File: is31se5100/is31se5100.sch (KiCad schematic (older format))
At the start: 1 part

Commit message: Added buttons to schematic
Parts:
- added C? (x6): 47nF, symbol Device:C_Small
- added R? (x6): 39k, symbol Device:R_Small
- added U? (x6): MAX7301, symbol Custom_Interface_Expansion:MAX7301
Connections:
- net labels added: BUTTON1, BUTTON10, BUTTON100, BUTTON101, BUTTON102, BUTTON103, BUTTON104, BUTTON105, BUTTON106, BUTTON107, BUTTON108, BUTTON109, BUTTON11, BUTTON110, BUTTON111, BUTTON112, BUTTON113, BUTTON114, BUTTON115, BUTTON116, BUTTON117, BUTTON118, BUTTON119, BUTTON12, BUTTON120, BUTTON121, BUTTON122, BUTTON123, BUTTON124, BUTTON125, BUTTON126, BUTTON127, BUTTON128, BUTTON129, BUTTON13, BUTTON130, BUTTON131, BUTTON132, BUTTON133, BUTTON134, BUTTON135, BUTTON136, BUTTON137, BUTTON138, BUTTON139, BUTTON14, BUTTON140, BUTTON141, BUTTON142, BUTTON143, BUTTON144, BUTTON15, BUTTON16, BUTTON17, BUTTON18, BUTTON19, BUTTON2, BUTTON20, BUTTON21, BUTTON22, BUTTON23, BUTTON24, BUTTON25, BUTTON26, BUTTON27, BUTTON28, BUTTON29, BUTTON3, BUTTON30, BUTTON31, BUTTON32, BUTTON33, BUTTON34, BUTTON35, BUTTON36, BUTTON37, BUTTON38, BUTTON39, BUTTON4, BUTTON40, BUTTON41, BUTTON42, BUTTON43, BUTTON44, BUTTON45, BUTTON46, BUTTON47, BUTTON48, BUTTON49, BUTTON5, BUTTON50, BUTTON51, BUTTON52, BUTTON53, BUTTON54, BUTTON55, BUTTON56, BUTTON57, BUTTON58, BUTTON59, BUTTON6, BUTTON60, BUTTON61, BUTTON62, BUTTON63, BUTTON64, BUTTON65, BUTTON66, BUTTON67, BUTTON68, BUTTON69, BUTTON7, BUTTON70, BUTTON71, BUTTON72, BUTTON73, BUTTON74, BUTTON75, BUTTON76, BUTTON77, BUTTON78, BUTTON79, BUTTON8, BUTTON80, BUTTON81, BUTTON82, BUTTON83, BUTTON84, BUTTON85, BUTTON86, BUTTON87, BUTTON88, BUTTON89, BUTTON9, BUTTON90, BUTTON91, BUTTON92, BUTTON93, BUTTON94, BUTTON95, BUTTON96, BUTTON97, BUTTON98, BUTTON99, SCKL, ~CS
- wire segments 0 -> 48
- no-connect marks 0 -> 24
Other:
- note added: "1 bulk decoupling capacitor\n"
- note added: "1 decoupling capactor 47nF per MAX7301"
- note added: "can leave disconnected output pins on the max7301 because of internal pull-ups\n"

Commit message: Added connections to IS31SE5100 and daisy-linked MAX7301s
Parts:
- removed U?: IS31SE5100, symbol Custom_Sensor_Touch:IS31SE5100
- added C?: 0.1uF, symbol Device:C_Small
- added C?: 10uF, symbol Device:C_Small
- added C? (x8): 5pF, symbol Device:C_Small
- added R? (x8): 510, symbol Device:R_Small
- added R? (x2): 10k, symbol Device:R_Small
- added R? (x2): 4k7, symbol Device:R_Small
- added U?: IS31SE5100-SALS2, symbol Custom_Sensor_Touch:IS31SE5100-SALS2
- added U? (x8): Electrode, symbol Custom_Sensor_Touch:Electrode
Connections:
- net labels added: BUTTON, INTB, MC_INTERRUPT, MC_SCL, MC_SDA, SCL, SDA, SDB
- wire segments 48 -> 142
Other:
- note added: "can leave unused output pins on the max7301 disconnected because of internal pull-ups\n"
- note removed: "can leave disconnected output pins on the max7301 because of internal pull-ups\n"
- moved on the sheet: R?, U?

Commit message: Added control test
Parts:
- added C?: 10uF, symbol Device:C_Small
- added C?: 0.1uF, symbol Device:C_Small
- added C? (x8): 5pF, symbol Device:C_Small
- added C?: 47nF, symbol Device:C_Small
- added D? (x8): G, symbol Device:LED_Small
- added J? (x2): Conn_01x04, symbol Connector_Generic:Conn_01x04
- added JP? (x2): SolderJumper_3_Bridged12, symbol Jumper:SolderJumper_3_Bridged12
- added R? (x8): 510, symbol Device:R_Small
- added R? (x5): 1k, symbol Device:R_Small
- added R? (x3): 4k7, symbol Device:R_Small
- added R?: 39k, symbol Device:R_Small
- added U?: IS31SE5100-SALS2, symbol Custom_Sensor_Touch:IS31SE5100-SALS2
- added U? (x8): Electrode, symbol Custom_Sensor_Touch:Electrode
- added U?: MAX7301, symbol Custom_Interface_Expansion:MAX7301
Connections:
- net +3V3: now also C?.1, C?.1, C?.1, D?.2 (A), D?.2 (A), D?.2 (A), D?.2 (A), D?.2 (A), D?.2 (A), D?.2 (A), D?.2 (A), U?.36 (Vdd), U?.5 (VCC)
- net GND: now also C?.2, C?.2, C?.2, C?.2, C?.2, C?.2, C?.2, C?.2, C?.2, C?.2, C?.2, R?.2, U?.14 (AD), U?.2 (GND), U?.22 (GND), U?.3 (GND), U?.4 (GND)
- new net: R?.2, U?.1 (OUT6)
- new net: R?.1, U?.10 (CAP8)
- new net: R?.1, U?.11 (CAP5)
- new net: R?.1, U?.12 (CAP6)
- new net: R?.1, U?.13 (CAP7)
- new net: R?.2, U?.19 (OUT1)
- new net: JP?.2 (C), U?.2 (OUT7)
- new net: R?.2, U?.20 (OUT2)
- new net: R?.2, U?.21 (OUT3)
- new net: R?.2, U?.23 (OUT4)
- new net: R?.2, U?.24 (OUT5)
- new net: JP?.2 (C), U?.3 (OUT8)
- new net: R?.1, U?.6 (CAP1)
- new net: R?.1, U?.7 (CAP2)
- new net: R?.1, U?.8 (CAP3)
- new net: R?.1, U?.9 (CAP4)
- new net: C?.1, R?.2, U?.~ (x8)
- new net: D?.1 (K), R?.1 (x8)
- new net: JP?.1 (A), R?.2 (x2)
- new net: R?.1, U?.1 (ISET)
- new net: JP?.3 (B), U?.30 (P5)
- new net: JP?.3 (B), U?.32 (P4)
- new net DIN_CTRL: J?.2 (Pin_2), U?.34 (DIN)
- new net DOUT_CTRL: J?.1 (Pin_1), U?.4 (DOUT)
- new net INTB_CTRL: J?.2 (Pin_2), U?.17 (INTB)
- new net SCKL_CTRL: J?.3 (Pin_3), U?.33 (SCKL)
- new net SCL_CTRL: J?.4 (Pin_4), U?.15 (SCL)
- new net SDA_CTRL: J?.3 (Pin_3), U?.16 (SDA)
- new net SDB_CTRL: J?.1 (Pin_1), U?.18 (SDB)
- new net ~CS_CTRL: J?.4 (Pin_4), U?.35 (~CS)
- no-connect marks 24 -> 50
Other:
- note added: "Control that tests one IS31SE5100 and one MAX7301 with jumpers\n"
- note added: "INTB is an interrupt line that is open drain"
- moved on the sheet: C?, R?, U?

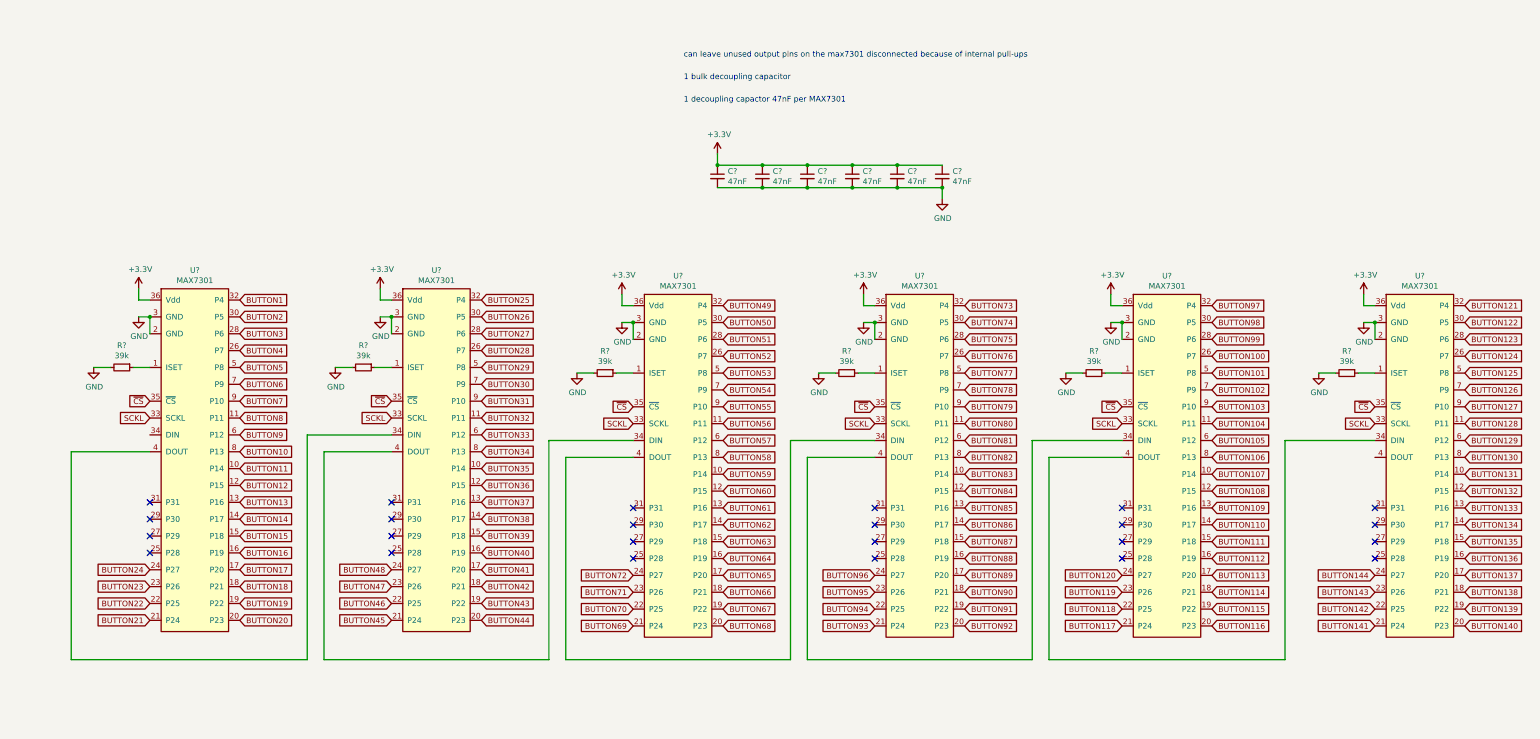
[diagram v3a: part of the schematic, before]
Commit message: Simplified by reducing number of IS31SE5100
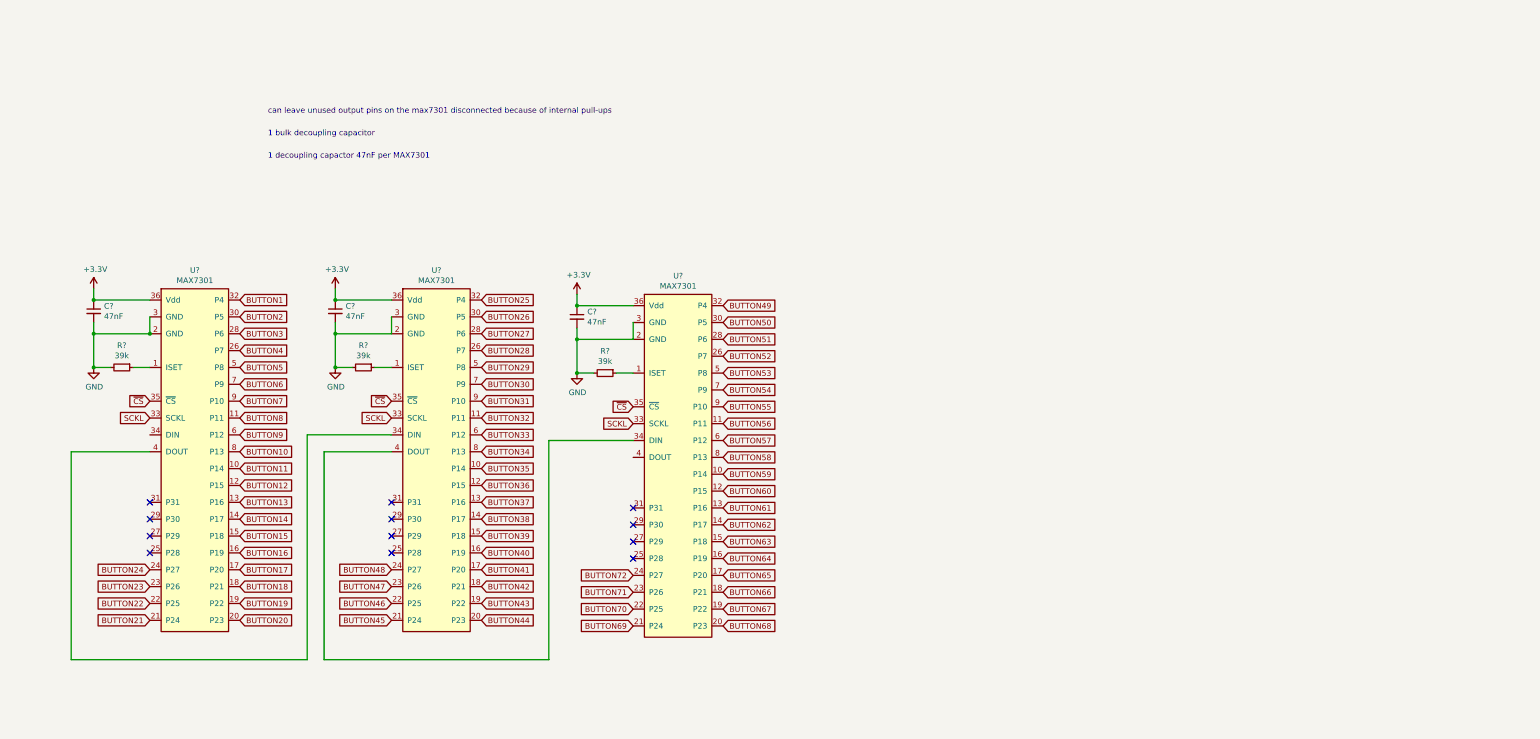
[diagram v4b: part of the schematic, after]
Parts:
- removed C? (x6): 47nF, symbol Device:C_Small
- removed R? (x6): 39k, symbol Device:R_Small
- removed U? (x3): MAX7301, symbol Custom_Interface_Expansion:MAX7301
- added C? (x3): 47nF, symbol Device:C_Small
- added R? (x3): 39k, symbol Device:R_Small
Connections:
- net +3V3: now also C?.1, C?.1, C?.1
- net GND: now also C?.2, C?.2, C?.2, R?.2, R?.2, R?.2
- net at U?.1 (ISET): now also R?.1 (x3)
- no-connect marks 50 -> 38

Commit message: Added pull-ups for I2C and INTB
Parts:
- removed R?: 10k, symbol Device:R_Small
- removed R? (x2): 4k7, symbol Device:R_Small
- added C? (x8): 10uF, symbol Device:C_Small
- added C? (x8): 0.1uF, symbol Device:C_Small
- added C? (x64): 5pF, symbol Device:C_Small
- added R? (x64): 510, symbol Device:R_Small
- added R? (x24): 4k7, symbol Device:R_Small
- added R? (x10): 10k, symbol Device:R_Small
- added R? (x2): 2k2, symbol Device:R_Small
- added U? (x8): IS31SE5100-SALS2, symbol Custom_Sensor_Touch:IS31SE5100-SALS2
- added U? (x64): Electrode, symbol Custom_Sensor_Touch:Electrode
- added U? (x3): PCA9546APW, symbol Custom_Interface_Expansion:PCA9546APW
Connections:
- net +3V3: now also C?.1, C?.1, C?.1, C?.1, C?.1, C?.1, C?.1, C?.1, C?.1, C?.1, C?.1, C?.1, C?.1, C?.1, C?.1, C?.1, R?.1, R?.1, R?.1, R?.1, R?.1, R?.1, R?.1, R?.1, R?.1, R?.1, R?.1, R?.1, R?.1, R?.1, R?.1, R?.1, R?.1, R?.1, R?.1, R?.1, R?.1, R?.1, R?.1, R?.1, R?.1, R?.1, R?.2, R?.2, R?.2, R?.2, R?.2, R?.2, R?.2, R?.2, R?.2, R?.2, U?.1 (A0), U?.16 (VDD), U?.16 (VDD), U?.16 (VDD), U?.2 (A1), U?.5 (VCC), U?.5 (VCC), U?.5 (VCC), U?.5 (VCC), U?.5 (VCC), U?.5 (VCC), U?.5 (VCC), U?.5 (VCC)
- net BUTTON1: now also U?.19 (OUT1)
- net BUTTON10: now also U?.20 (OUT2)
- net BUTTON11: now also U?.21 (OUT3)
- net BUTTON12: now also U?.23 (OUT4)
- net BUTTON13: now also U?.24 (OUT5)
- net BUTTON14: now also U?.1 (OUT6)
- net BUTTON15: now also U?.2 (OUT7)
- net BUTTON16: now also U?.3 (OUT8)
- net BUTTON17: now also U?.19 (OUT1)
- net BUTTON18: now also U?.20 (OUT2)
- net BUTTON19: now also U?.21 (OUT3)
- net BUTTON2: now also U?.20 (OUT2)
- net BUTTON20: now also U?.23 (OUT4)
- net BUTTON21: now also U?.24 (OUT5)
- net BUTTON22: now also U?.1 (OUT6)
- net BUTTON23: now also U?.2 (OUT7)
- net BUTTON24: now also U?.3 (OUT8)
- net BUTTON25: now also U?.19 (OUT1)
- net BUTTON26: now also U?.20 (OUT2)
- net BUTTON27: now also U?.21 (OUT3)
- net BUTTON28: now also U?.23 (OUT4)
- net BUTTON29: now also U?.24 (OUT5)
- net BUTTON3: now also U?.21 (OUT3)
- net BUTTON30: now also U?.1 (OUT6)
- net BUTTON31: now also U?.2 (OUT7)
- net BUTTON32: now also U?.3 (OUT8)
- net BUTTON33: now also U?.19 (OUT1)
- net BUTTON34: now also U?.20 (OUT2)
- net BUTTON35: now also U?.21 (OUT3)
- net BUTTON36: now also U?.23 (OUT4)
- net BUTTON37: now also U?.24 (OUT5)
- net BUTTON38: now also U?.1 (OUT6)
- net BUTTON39: now also U?.2 (OUT7)
- net BUTTON4: now also U?.23 (OUT4)
- net BUTTON40: now also U?.3 (OUT8)
- net BUTTON41: now also U?.19 (OUT1)
- net BUTTON42: now also U?.20 (OUT2)
- net BUTTON43: now also U?.21 (OUT3)
- net BUTTON44: now also U?.23 (OUT4)
- net BUTTON45: now also U?.24 (OUT5)
- net BUTTON46: now also U?.1 (OUT6)
- net BUTTON47: now also U?.2 (OUT7)
- net BUTTON48: now also U?.3 (OUT8)
- net BUTTON49: now also U?.19 (OUT1)
- net BUTTON5: now also U?.24 (OUT5)
- net BUTTON50: now also U?.20 (OUT2)
- net BUTTON51: now also U?.21 (OUT3)
- net BUTTON52: now also U?.23 (OUT4)
- net BUTTON53: now also U?.24 (OUT5)
- net BUTTON54: now also U?.1 (OUT6)
- net BUTTON55: now also U?.2 (OUT7)
- net BUTTON56: now also U?.3 (OUT8)
- net BUTTON57: now also U?.19 (OUT1)
- net BUTTON58: now also U?.20 (OUT2)
- net BUTTON59: now also U?.21 (OUT3)
- net BUTTON6: now also U?.1 (OUT6)
- net BUTTON60: now also U?.23 (OUT4)
- net BUTTON61: now also U?.24 (OUT5)
- net BUTTON62: now also U?.1 (OUT6)
- net BUTTON63: now also U?.2 (OUT7)
- net BUTTON64: now also U?.3 (OUT8)
- net BUTTON65: now also U?.19 (OUT1)
- net BUTTON66: now also U?.20 (OUT2)
- net BUTTON67: now also U?.21 (OUT3)
- net BUTTON68: now also U?.23 (OUT4)
- net BUTTON69: now also U?.24 (OUT5)
- net BUTTON7: now also U?.2 (OUT7)
- net BUTTON70: now also U?.1 (OUT6)
- net BUTTON71: now also U?.2 (OUT7)
- net BUTTON72: now also U?.3 (OUT8)
- net BUTTON8: now also U?.3 (OUT8)
- net BUTTON9: now also U?.19 (OUT1)
- net GND: now also C?.2, C?.2, C?.2, C?.2, C?.2, C?.2, C?.2, C?.2, C?.2, C?.2, C?.2, C?.2, C?.2, C?.2, C?.2, C?.2, C?.2, C?.2, C?.2, C?.2, C?.2, C?.2, C?.2, C?.2, C?.2, C?.2, C?.2, C?.2, C?.2, C?.2, C?.2, C?.2, C?.2, C?.2, C?.2, C?.2, C?.2, C?.2, C?.2, C?.2, C?.2, C?.2, C?.2, C?.2, C?.2, C?.2, C?.2, C?.2, C?.2, C?.2, C?.2, C?.2, C?.2, C?.2, C?.2, C?.2, C?.2, C?.2, C?.2, C?.2, C?.2, C?.2, C?.2, C?.2, C?.2, C?.2, C?.2, C?.2, C?.2, C?.2, C?.2, C?.2, C?.2, C?.2, C?.2, C?.2, C?.2, C?.2, C?.2, C?.2, U?.1 (A0), U?.1 (A0), U?.13 (A2), U?.13 (A2), U?.13 (A2), U?.14 (AD), U?.14 (AD), U?.14 (AD), U?.14 (AD), U?.14 (AD), U?.14 (AD), U?.14 (AD), U?.14 (AD), U?.2 (A1), U?.2 (A1), U?.22 (GND), U?.22 (GND), U?.22 (GND), U?.22 (GND), U?.22 (GND), U?.22 (GND), U?.22 (GND), U?.22 (GND), U?.4 (GND), U?.4 (GND), U?.4 (GND), U?.4 (GND), U?.4 (GND), U?.4 (GND), U?.4 (GND), U?.4 (GND), U?.8 (VSS), U?.8 (VSS), U?.8 (VSS)
- net SDB_CTRL: no longer U?.18 (SDB)
- removed net BUTTON: U?.1 (OUT6), U?.19 (OUT1), U?.2 (OUT7), U?.20 (OUT2), U?.21 (OUT3), U?.23 (OUT4), U?.24 (OUT5), U?.3 (OUT8)
- net INTB renamed INTB1
- net INTB1: now also U?.17 (INTB), U?.17 (INTB), U?.17 (INTB), U?.17 (INTB), U?.17 (INTB), U?.17 (INTB), U?.17 (INTB), U?.17 (INTB)
- net MC_SCL renamed M_SCL1
- net M_SCL1: now also R?.2, U?.5 (SC0)
- net MC_SDA renamed M_SDA1
- net M_SDA1: now also R?.2, U?.4 (SD0)
- net SDB: no longer names the net of U?.18 (SDB)
- net SDB: now also R?.1
- new net: R?.1, U?.18 (SDB) (x9)
- new net: R?.1, U?.10 (CAP8) (x8)
- new net: R?.1, U?.11 (CAP5) (x8)
- new net: R?.1, U?.12 (CAP6) (x8)
- new net: R?.1, U?.13 (CAP7) (x8)
- new net: R?.1, U?.6 (CAP1) (x8)
- new net: R?.1, U?.7 (CAP2) (x8)
- new net: R?.1, U?.8 (CAP3) (x8)
- new net: R?.1, U?.9 (CAP4) (x8)
- new net: C?.1, R?.2, U?.~ (x64)
- new net: R?.2, U?.11 (SD3) (x3)
- new net: R?.2, U?.12 (SC3) (x3)
- new net M_SCL2: R?.2, U?.15 (SCL), U?.6 (SD1)
- new net M_SCL3: R?.2, U?.10 (SC2), U?.15 (SCL)
- new net M_SCL4: R?.2, U?.15 (SCL), U?.5 (SC0)
- new net M_SCL5: R?.2, U?.15 (SCL), U?.6 (SD1)
- new net M_SCL6: R?.2, U?.10 (SC2), U?.15 (SCL)
- new net M_SCL7: R?.2, U?.15 (SCL), U?.5 (SC0)
- new net M_SCL8: R?.2, U?.15 (SCL), U?.6 (SD1)
- new net M_SCL9: R?.2, U?.10 (SC2), U?.15 (SCL)
- new net M_SDA2: R?.2, U?.16 (SDA), U?.7 (SC1)
- new net M_SDA3: R?.2, U?.16 (SDA), U?.9 (SD2)
- new net M_SDA4: R?.2, U?.16 (SDA), U?.4 (SD0)
- new net M_SDA5: R?.2, U?.16 (SDA), U?.7 (SC1)
- new net M_SDA6: R?.2, U?.16 (SDA), U?.9 (SD2)
- new net M_SDA7: R?.2, U?.16 (SDA), U?.4 (SD0)
- new net M_SDA8: R?.2, U?.16 (SDA), U?.7 (SC1)
- new net M_SDA9: R?.2, U?.16 (SDA), U?.9 (SD2)
- new net SCL1: R?.2, U?.14 (SCL), U?.14 (SCL), U?.14 (SCL)
- new net SDA1: R?.2, U?.15 (SDA), U?.15 (SDA), U?.15 (SDA)
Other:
- note added: "1 bulk decoupling capacitor (each?)\n"
- note added: "STM32L476RG is 3.3V and we want possible I2C Fast Mode"
- note removed: "1 bulk decoupling capacitor\n"
- moved on the sheet: C?, D?, J?, JP?, R?, U?

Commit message: Preparation for power
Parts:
- removed J?: Conn_01x04, symbol Connector_Generic:Conn_01x04
- added D?: G, symbol Device:LED_Small
- added J?: Conn_01x03, symbol Connector_Generic:Conn_01x03
- added R?: 1k, symbol Device:R_Small
- added R? (x2): 2k2, symbol Device:R_Small
- D? (x8): value G -> Y
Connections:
- net +3V3: now also D?.2 (A), R?.1, R?.1
- net GND: now also R?.2
- net INTB_CTRL: now also J?.1 (Pin_1)
- net SCL_CTRL: now also J?.3 (Pin_3), R?.2
- net SDA_CTRL: now also J?.2 (Pin_2), R?.2
- new net: D?.1 (K), R?.1
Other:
- note added: "1 bulk decoupling capacitor?\n"
- note added: "Power supply"
- note removed: "1 bulk decoupling capacitor (each?)\n"
- moved on the sheet: C?, D?, J?, JP?, R?, U?

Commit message: Added power circuit and extraneous parts
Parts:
- removed C? (x72): 5pF, symbol Device:C_Small
- removed D?: G, symbol Device:LED_Small
- removed R? (x27): 4k7, symbol Device:R_Small
- removed R?: 1k, symbol Device:R_Small
- removed U? (x8): Electrode, symbol Custom_Sensor_Touch:Electrode
- added C? (x10): 10nF, symbol Device:C_Small
- added C? (x14): 10uF, symbol Device:C_Small
- added C? (x8): 5pF, symbol Device:C_Small
- added C? (x8): 10pF, symbol Device:C_Small
- added C? (x8): 15pF, symbol Device:C_Small
- added C? (x8): 1nF, symbol Device:C_Small
- added C? (x8): 5nF, symbol Device:C_Small
- added C? (x8): 1pF, symbol Device:C_Small
- added C? (x8): 15nF, symbol Device:C_Small
- added C? (x8): 25nF, symbol Device:C_Small
- added C? (x8): 50nF, symbol Device:C_Small
- added C? (x8): 1uF, symbol Device:C_Small
- added C? (x8): 5uF, symbol Device:C_Small
- added C? (x8): 15uF, symbol Device:C_Small
- added C? (x8): 25uF, symbol Device:C_Small
- added C? (x8): 50uF, symbol Device:C_Small
- added C? (x72): 6pF, symbol Device:C_Small
- added C? (x8): 100nF, symbol Device:C_Small
- added C? (x8): 20pF, symbol Device:C_Small
- added C? (x8): 22pF, symbol Device:C_Small
- added C? (x8): 18pF, symbol Device:C_Small
- added D?: G, symbol Device:LED_Small
- added D? (x4): B5819W, symbol Device:D_Schottky_Small
- added D?: B, symbol Device:LED_Small
- added F? (x2): 250mA, symbol Device:Polyfuse_Small
- added FB? (x2): 600 @ 600MHz, symbol Device:Ferrite_Bead_Small
- added J? (x16): Conn_01x08, symbol Connector_Generic:Conn_01x08
- added J?: Conn_01x04, symbol Connector_Generic:Conn_01x04
- added JP? (x14): SolderJumper_3_Bridged12, symbol Jumper:SolderJumper_3_Bridged12
- added L? (x2): 10uH, symbol Device:L_Small
- added Q? (x2): AO3401A, Package_TO_SOT_SMD:SOT-23, symbol Transistor_FET:AO3401A
- added R? (x13): 1k, symbol Device:R_Small
- added R? (x36): 2k2, symbol Device:R_Small
- added R? (x10): 100k, symbol Device:R_Small
- added R? (x2): 68k, symbol Device:R_Small
- added R? (x10): 47k, symbol Device:R_Small
- added R? (x10): 15k, symbol Device:R_Small
- added R? (x10): 270, symbol Device:R_Small
- added R? (x8): 1, symbol Device:R_Small
- added R? (x8): 10, symbol Device:R_Small
- added R? (x8): 100, symbol Device:R_Small
- added R? (x8): 10k, symbol Device:R_Small
- added R? (x8): 1.5, symbol Device:R_Small
- added R? (x8): 15, symbol Device:R_Small
- added R? (x8): 150, symbol Device:R_Small
- added R? (x8): 1k5, symbol Device:R_Small
- added R? (x8): 150k, symbol Device:R_Small
- added R? (x8): 2.2, symbol Device:R_Small
- added R? (x8): 22, symbol Device:R_Small
- added R? (x8): 220, symbol Device:R_Small
- added R? (x8): 22k, symbol Device:R_Small
- added R? (x8): 220k, symbol Device:R_Small
- added R? (x8): 2.7, symbol Device:R_Small
- added R? (x8): 27, symbol Device:R_Small
- added R? (x8): 2k7, symbol Device:R_Small
- added R? (x8): 27k, symbol Device:R_Small
- added R? (x8): 270k, symbol Device:R_Small
- added R? (x8): 3.3, symbol Device:R_Small
- added R? (x8): 33, symbol Device:R_Small
- added R? (x8): 330, symbol Device:R_Small
- added R? (x8): 3k3, symbol Device:R_Small
- added R? (x8): 33k, symbol Device:R_Small
- added R? (x8): 330k, symbol Device:R_Small
- added R? (x8): 3.9, symbol Device:R_Small
- added R? (x8): 39, symbol Device:R_Small
- added R? (x8): 390, symbol Device:R_Small
- added R? (x8): 3k9, symbol Device:R_Small
- added R? (x8): 39k, symbol Device:R_Small
- added R? (x8): 390k, symbol Device:R_Small
- added R? (x8): 4.7, symbol Device:R_Small
- added R? (x8): 47, symbol Device:R_Small
- added R? (x8): 470, symbol Device:R_Small
- added R? (x8): 4k7, symbol Device:R_Small
- added R? (x8): 470k, symbol Device:R_Small
- added R? (x8): 5.1, symbol Device:R_Small
- added R? (x8): 51, symbol Device:R_Small
- added R? (x8): 510, symbol Device:R_Small
- added R? (x8): 5k1, symbol Device:R_Small
- added R? (x8): 51k, symbol Device:R_Small
- added R? (x8): 510k, symbol Device:R_Small
- added R? (x8): 120, symbol Device:R_Small
- added R? (x8): 180, symbol Device:R_Small
- added R? (x8): 250, symbol Device:R_Small
- added R? (x8): 300, symbol Device:R_Small
- added R? (x8): 360, symbol Device:R_Small
- added R? (x8): 430, symbol Device:R_Small
- added R? (x8): 1M, symbol Device:R_Small
- added R? (x8): 0, symbol Device:R_Small
- added U? (x128): Electrode, symbol Custom_Sensor_Touch:Electrode
- added U? (x2): MP2359DT-LF, symbol Custom_Power:MP2359DT-LF
- C? (x8): value 5pF -> 6pF
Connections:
- net +3V3: now also C?.1, C?.1, D?.2 (A), L?.2, R?.1, R?.1, R?.1, R?.1, R?.1, R?.1, R?.1, R?.1, R?.1, R?.1, R?.1, R?.1, R?.1, R?.1, R?.1, R?.1, R?.1, R?.1, R?.1, R?.1, R?.1, R?.1, R?.1, R?.1, R?.1, R?.1, R?.1, R?.1, R?.1; no longer C?.1, C?.1, C?.1, D?.2 (A), D?.2 (A), D?.2 (A), D?.2 (A), D?.2 (A), D?.2 (A), D?.2 (A), D?.2 (A), R?.1, R?.1, U?.36 (Vdd), U?.5 (VCC)
- net GND: now also C?.2, C?.2, C?.2, C?.2, C?.2, C?.2, C?.2, C?.2, C?.2, C?.2, C?.2, C?.2, C?.2, C?.2, C?.2, C?.2, C?.2, C?.2, C?.2, C?.2, C?.2, C?.2, C?.2, C?.2, C?.2, C?.2, C?.2, C?.2, C?.2, C?.2, C?.2, C?.2, C?.2, C?.2, C?.2, C?.2, C?.2, C?.2, C?.2, C?.2, C?.2, C?.2, C?.2, C?.2, C?.2, C?.2, C?.2, C?.2, C?.2, C?.2, C?.2, C?.2, C?.2, C?.2, C?.2, C?.2, C?.2, C?.2, C?.2, C?.2, C?.2, C?.2, C?.2, C?.2, C?.2, C?.2, C?.2, C?.2, C?.2, C?.2, C?.2, C?.2, C?.2, C?.2, C?.2, D?.2 (A), Q?.1 (G), R?.2, R?.2, R?.2, U?.2 (GND); no longer C?.2, C?.2, C?.2, C?.2, C?.2, C?.2, C?.2, C?.2, C?.2, R?.2, U?.14 (AD), U?.2 (GND), U?.22 (GND), U?.3 (GND), U?.4 (GND)
- net INTB_CTRL: now also R?.2
- net M_SCL1: now also R?.2
- net M_SCL2: now also R?.2
- net M_SCL3: now also R?.2
- net M_SCL4: now also R?.2
- net M_SCL5: now also R?.2
- net M_SCL6: now also R?.2
- net M_SCL7: now also R?.2
- net M_SCL8: now also R?.2
- net M_SCL9: now also R?.2
- net M_SDA1: now also R?.2
- net M_SDA2: now also R?.2
- net M_SDA3: now also R?.2
- net M_SDA4: now also R?.2
- net M_SDA5: now also R?.2
- net M_SDA6: now also R?.2
- net M_SDA7: now also R?.2
- net M_SDA8: now also R?.2
- net M_SDA9: now also R?.2
- net SCKL: now also J?.2 (Pin_2)
- net SCL_CTRL: now also R?.2; no longer R?.2
- net SDA_CTRL: now also R?.2; no longer R?.2
- net ~CS: now also J?.1 (Pin_1)
- net DIN: now reaches U?.34 (DIN)
- net DIN: now also J?.3 (Pin_3)
- net DOUT: now reaches U?.4 (DOUT)
- net DOUT: now also J?.4 (Pin_4)
- net at R?.2, U?.~: now also C?.1 (x72)
- net at U?.1 (OUT6): now also JP?.2 (C)
- net at U?.19 (OUT1): now also JP?.2 (C); no longer R?.2
- net at U?.20 (OUT2): now also JP?.2 (C); no longer R?.2
- net at U?.21 (OUT3): now also JP?.2 (C); no longer R?.2
- net at U?.23 (OUT4): now also JP?.2 (C); no longer R?.2
- net at U?.24 (OUT5): now also JP?.2 (C); no longer R?.2
- net ELECTRODE8: now reaches C?.1, R?.2
- net ELECTRODE8: now also JP?.1 (A)
- net ELECTRODE2: now reaches C?.1, R?.2
- net ELECTRODE2: now also JP?.1 (A)
- net ELECTRODE1: now reaches C?.1, R?.2
- net ELECTRODE1: now also JP?.1 (A)
- net ELECTRODE3: now reaches C?.1, R?.2
- net ELECTRODE3: now also JP?.1 (A)
- net ELECTRODE4: now reaches C?.1, R?.2
- net ELECTRODE4: now also JP?.1 (A)
- net ELECTRODE5: now reaches C?.1, R?.2
- net ELECTRODE5: now also JP?.1 (A)
- net ELECTRODE6: now reaches C?.1, R?.2
- net ELECTRODE6: now also JP?.1 (A)
- net ELECTRODE7: now reaches C?.1, R?.2
- net ELECTRODE7: now also JP?.1 (A)
- net at D?.1 (K): now also R?.1 (x3)
- net at JP?.1 (A): now also R?.2 (x2)
- net at U?.11 (P11): now also JP?.3 (B)
- net at U?.26 (P7): now also JP?.3 (B)
- net at U?.28 (P6): now also JP?.3 (B)
- net at U?.30 (P5): now also JP?.3 (B); no longer JP?.3 (B)
- net at U?.32 (P4): now also JP?.3 (B); no longer JP?.3 (B)
- net at U?.5 (P8): now also JP?.3 (B)
- net at U?.7 (P9): now also JP?.3 (B)
- net at U?.9 (P10): now also JP?.3 (B)
- net at U?.11 (SD3): now also R?.2 (x3)
- net at U?.12 (SC3): now also R?.2 (x3)
- net at U?.3 (~RESET): now also R?.2 (x3)
- new net: JP?.2 (C), U?.~ (x8)
- new net: C?.1, C?.1, U?.5 (VCC)
- new net: U?.14 (AD), U?.22 (GND), U?.4 (GND)
- new net: C?.2, C?.2, C?.2, C?.2, C?.2, C?.2, C?.2, C?.2
- new net: D?.2 (A), D?.2 (A), D?.2 (A), D?.2 (A), D?.2 (A), D?.2 (A), D?.2 (A), D?.2 (A)
- new net: JP?.1 (A), R?.2 (x6)
- new net: C?.1, U?.36 (Vdd)
- new net: D?.1 (K), R?.1 (x2)
- new net: R?.1, R?.2 (x2)
- new net: F?.1, FB?.2 (x2)
- new net: D?.1 (K), F?.2, Q?.2 (S) (x2)
- new net: C?.1, C?.1, L?.2
- new net: J?.1 (Pin_1), U?.~ (x15)
- new net: J?.2 (Pin_2), U?.~ (x15)
- new net: J?.3 (Pin_3), U?.~ (x15)
- new net: J?.4 (Pin_4), U?.~ (x15)
- new net: J?.5 (Pin_5), U?.~ (x15)
- new net: J?.6 (Pin_6), U?.~ (x15)
- new net: J?.7 (Pin_7), U?.~ (x15)
- new net: J?.8 (Pin_8), U?.~ (x15)
- new net +5V: D?.2 (A)
- new net +9V: Q?.3 (D)
- new net ALT1: J?.1 (Pin_1), JP?.3 (B)
- new net ALT2: J?.2 (Pin_2), JP?.3 (B)
- new net ALT3: J?.3 (Pin_3), JP?.3 (B)
- new net ALT4: J?.4 (Pin_4), JP?.3 (B)
- new net ALT5: J?.5 (Pin_5), JP?.3 (B)
- new net ALT6: J?.6 (Pin_6), JP?.3 (B)
- new net ALT7: J?.7 (Pin_7), JP?.3 (B)
- new net ALT8: J?.8 (Pin_8), JP?.3 (B)
- new net BUCK_BST: C?.1, U?.1 (BST)
- new net BUCK_BST_CTRL: C?.1, U?.1 (BST)
- new net BUCK_EN: R?.1, R?.2, U?.4 (EN)
- new net BUCK_EN_CTRL: R?.1, R?.2, U?.4 (EN)
- new net BUCK_FB: R?.1, R?.2, U?.3 (FB)
- new net BUCK_FB_CTRL: R?.1, R?.2, U?.3 (FB)
- new net BUCK_IN: C?.1, FB?.1, R?.1, U?.5 (IN)
- new net BUCK_IN_CTRL: C?.1, FB?.1, R?.1, U?.5 (IN)
- new net BUCK_SW: C?.2, D?.1 (K), L?.1, U?.6 (SW)
- new net BUCK_SW_CTRL: C?.2, D?.1 (K), L?.1, U?.6 (SW)
- new net GND1: C?.2, R?.2, U?.2 (GND), U?.3 (GND)
- no-connect marks 38 -> 1232
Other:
- note added: "Alternative electrodes to test based on sizes"
- note added: "IS31SE5100 does not source from its output; only sinks. that makes sense because the outputs are either pull down (sink) or floating (disconnect/no source)."
- note added: "can leave unused output pins on the max7301 disconnected because of internal pull-ups. \n\ninternal pull-ups also measn we can connect the is31se5100 directly to the buttons as they are open collector\n"
- note removed: "can leave unused output pins on the max7301 disconnected because of internal pull-ups\n"
- moved on the sheet: C?, D?, J?, JP?, R?, U?

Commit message: Simplified by removing one more is31se5100
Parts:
- removed C?: 47nF, symbol Device:C_Small
- removed C? (x3): 10uF, symbol Device:C_Small
- removed C? (x3): 0.1uF, symbol Device:C_Small
- removed C? (x24): 6pF, symbol Device:C_Small
- removed R?: 39k, symbol Device:R_Small
- removed R? (x24): 510, symbol Device:R_Small
- removed R? (x3): 10k, symbol Device:R_Small
- removed R? (x9): 2k2, symbol Device:R_Small
- removed U?: MAX7301, symbol Custom_Interface_Expansion:MAX7301
- removed U? (x3): IS31SE5100-SALS2, symbol Custom_Sensor_Touch:IS31SE5100-SALS2
- removed U? (x24): Electrode, symbol Custom_Sensor_Touch:Electrode
- removed U?: PCA9546APW, symbol Custom_Interface_Expansion:PCA9546APW
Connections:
- net DOUT: now also U?.4 (DOUT)
- no-connect marks 1232 -> 1228
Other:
- moved on the sheet: C?, D?, F?, FB?, J?, JP?, L?, Q?, R?, U?
